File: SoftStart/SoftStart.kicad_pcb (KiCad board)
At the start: 2 copper layers, 88 x 56 mm, 26 parts, among them J1 LIVE, J10 LIVE, J2 NEUTRAL, J3 SW1, J4 SW2, J5 NEUTRAL, J6 SWOUTPUT, J7 LIVE, J8 LIVE, J9 LIVE

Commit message: Submitted to JLCPCB 2020-08-24
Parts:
- moved R3 1.00 mm to (159.0, 41.0)
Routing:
- net Net-(C1-Pad2): track 127.0 -> 126.1 mm
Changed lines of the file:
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@@
     (links 34)
     (no_connects 0)
-    (area 95.924999 24.924999 184.075001 81.075001)
+    (area 95.924999 24.924999 184.075001 81.200002)
     (thickness 1.6)
     (drawings 11)
@@
   )
   (setup
-    (last_trace_width 2)
+    (last_trace_width 0.25)
     (user_trace_width 0.5)
     (user_trace_width 1)
@@
     (pad_to_mask_clearance 0.2)
     (aux_axis_origin 0 0)
-    (visible_elements FFFFFF7F)
+    (visible_elements 7FFFFFFF)
     (pcbplotparams
       (layerselection 0x010f0_80000001)
@@
   )
   (module Resistors_THT:R_Axial_Power_L20.0mm_W6.4mm_P22.40mm (layer F.Cu)
-    (at 159 40)
+    (at 159 41)
     (descr "Resistor, Axial_Power series, Axial, Horizontal, pin pitch=22.4mm, 4W, length*diameter=20*6.4mm^2, http://cdn-reichelt.de/documents/datenblatt/B400/5WAXIAL_9WAXIAL_11WAXIAL_17WAXIAL%23YAG.pdf")
     (tags "Resistor Axial_Power series Axial Horizontal pin pitch 22.4mm 4W length 20mm diameter 6.4mm")
@@
   (segment (start 181.4 57) (end 181.4 65) (width 4) (layer B.Cu) (net 2))
   (segment (start 181.4 49) (end 181.4 57) (width 4) (layer B.Cu) (net 2))
-  (segment (start 181.4 40) (end 181.4 49) (width 4) (layer B.Cu) (net 2))
+  (segment (start 181.4 41) (end 181.4 49) (width 4) (layer B.Cu) (net 2) (status 10))
   (segment (start 152.8 28.6) (end 163.6 28.6) (width 4) (layer B.Cu) (net 2))
   (segment (start 163.6 28.6) (end 175 40) (width 4) (layer B.Cu) (net 2))
-  (segment (start 175 40) (end 181.4 40) (width 4) (layer B.Cu) (net 2))
+  (segment (start 175 40) (end 181.4 41) (width 4) (layer B.Cu) (net 2) (status 20))
   (segment (start 145.2 28.6) (end 152.8 28.6) (width 4) (layer B.Cu) (net 2))
   (segment (start 108 35) (end 108 34) (width 4) (layer B.Cu) (net 2) (status 30))
@@
   (segment (start 152.8 33.68) (end 156.68 33.68) (width 2) (layer B.Cu) (net 9))
   (segment (start 156.68 33.68) (end 159 36) (width 2) (layer B.Cu) (net 9))
-  (segment (start 159 36) (end 159 40) (width 2) (layer B.Cu) (net 9))
+  (segment (start 159 36) (end 159 41) (width 2) (layer B.Cu) (net 9) (status 20))
   (segment (start 159 49) (end 159 57) (width 4) (layer B.Cu) (net 9))
-  (segment (start 159 40) (end 159 46) (width 4) (layer B.Cu) (net 9))
+  (segment (start 159 41) (end 159 46) (width 4) (layer B.Cu) (net 9) (status 10))
   (segment (start 159 46) (end 159 49) (width 4) (layer B.Cu) (net 9))
   (segment (start 159 57) (end 159 65) (width 4) (layer B.Cu) (net 9))

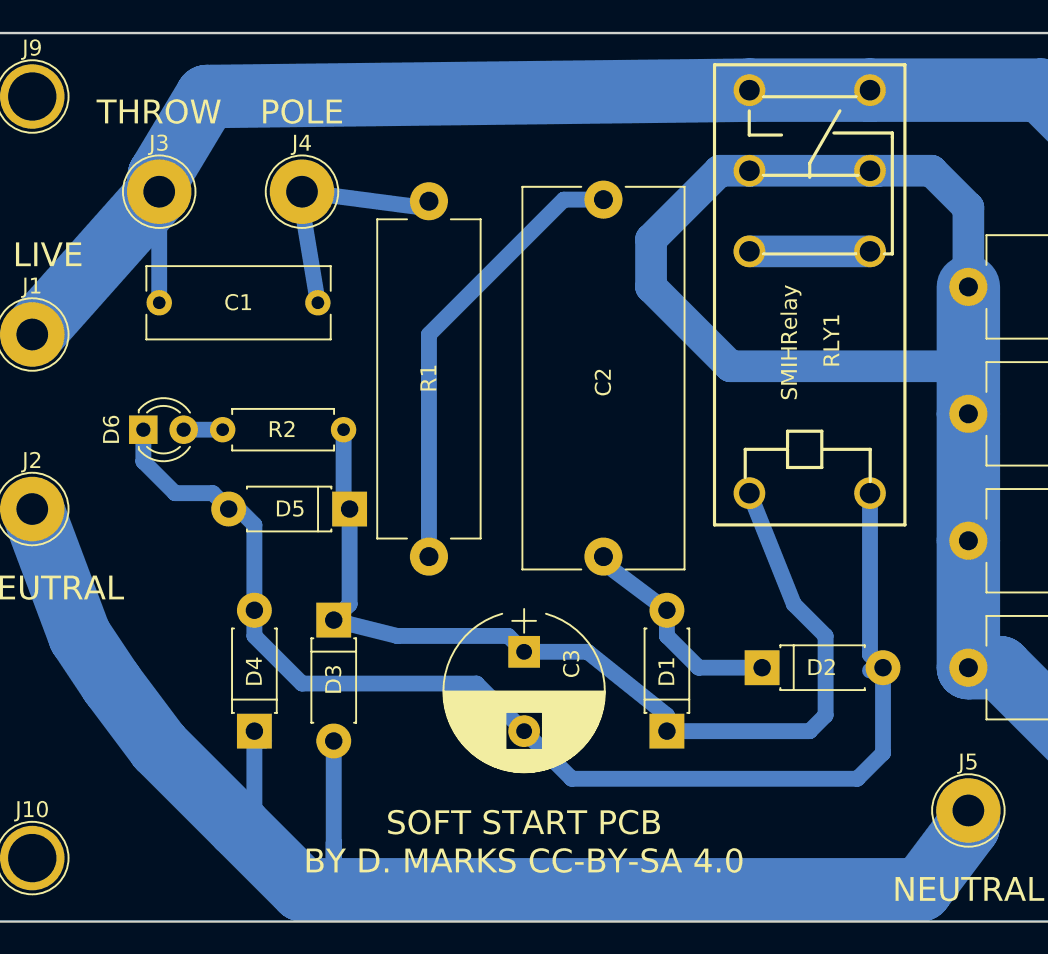
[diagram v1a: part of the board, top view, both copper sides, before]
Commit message: Fixed nasty bug in soft start
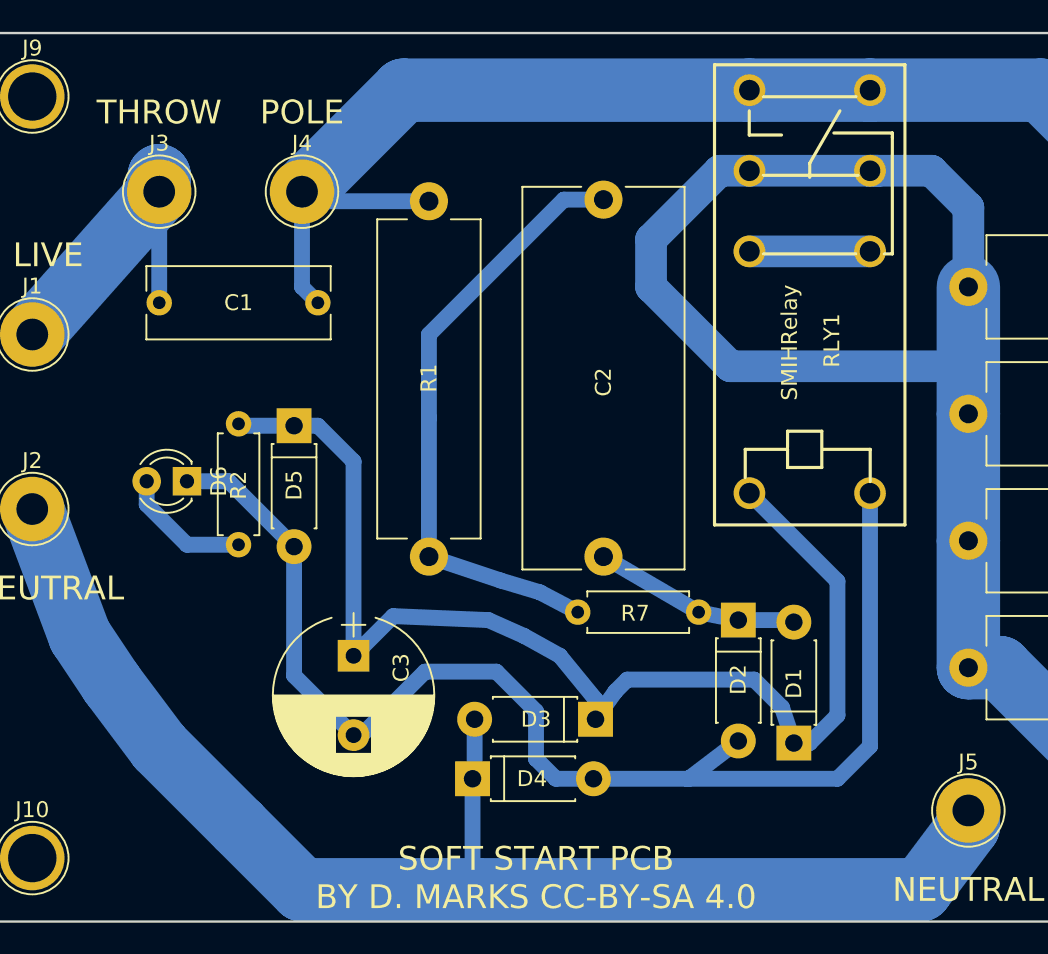
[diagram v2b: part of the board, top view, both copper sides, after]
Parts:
- added R7: 1M, Resistors_THT:R_Axial_DIN0207_L6.3mm_D2.5mm_P7.62mm_Horizontal, F.Cu at (142.0, 61.5)
- R3, R4, R5, R6: value 220R -> 150R
- moved D3 17.6 mm to (135.5, 68.2), turned to 180 degrees
- moved D4 14.1 mm to (127.8, 72.0), turned to 0 degrees
- moved C3 10.8 mm to (120.2, 64.2)
- moved D1 8.04 mm to (148.0, 69.8)
- moved R2 7.32 mm to (113.0, 57.2), turned to 90 degrees
- moved D5 6.31 mm to (116.5, 49.8), turned to 270 degrees
- moved D6 4.26 mm to (109.8, 53.2), turned to 180 degrees
- moved D2 3.35 mm to (144.5, 62.0), turned to 270 degrees
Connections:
- R3 pad 2: Net-(C1-Pad2) -> Net-(C1-Pad1)
- R4 pad 2: Net-(C1-Pad2) -> Net-(C1-Pad1)
- R5 pad 2: Net-(C1-Pad2) -> Net-(C1-Pad1)
- R6 pad 2: Net-(C1-Pad2) -> Net-(C1-Pad1)
- RLY1 pad 3: Net-(C1-Pad2) -> Net-(C1-Pad1)
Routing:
- net Net-(C1-Pad2): track 126.1 -> 21.0 mm
- net Net-(C1-Pad1): track 15.9 -> 113.1 mm
- net Net-(C3-Pad1): track 62.3 -> 75.7 mm
- net Net-(D3-Pad2): track 101.0 -> 89.2 mm
- net Net-(C2-Pad2): track 28.5 -> 39.1 mm
- net Net-(D6-Pad2): track 2.46 -> 8.30 mm
- net Net-(C3-Pad2): track 79.2 -> 81.9 mm

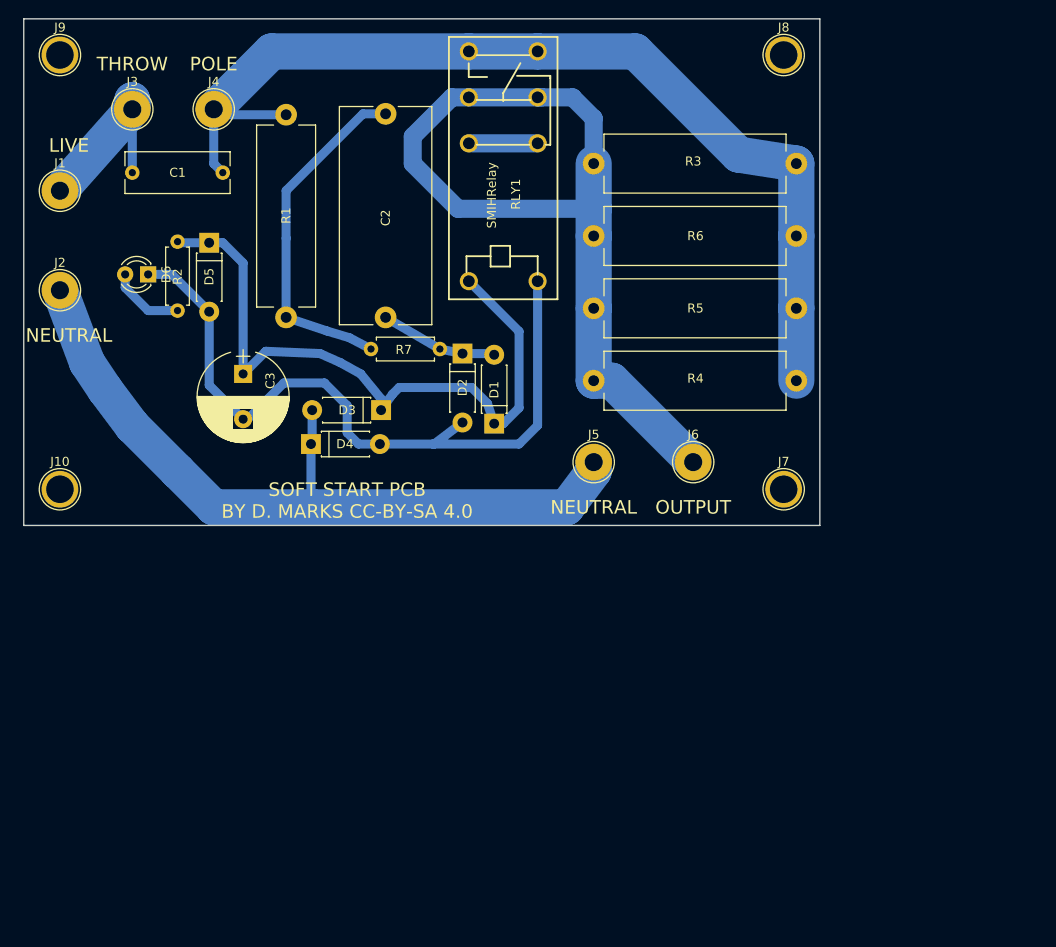
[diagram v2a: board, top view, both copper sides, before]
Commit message: Changed softstart and Poweramp to TO-220 transistors
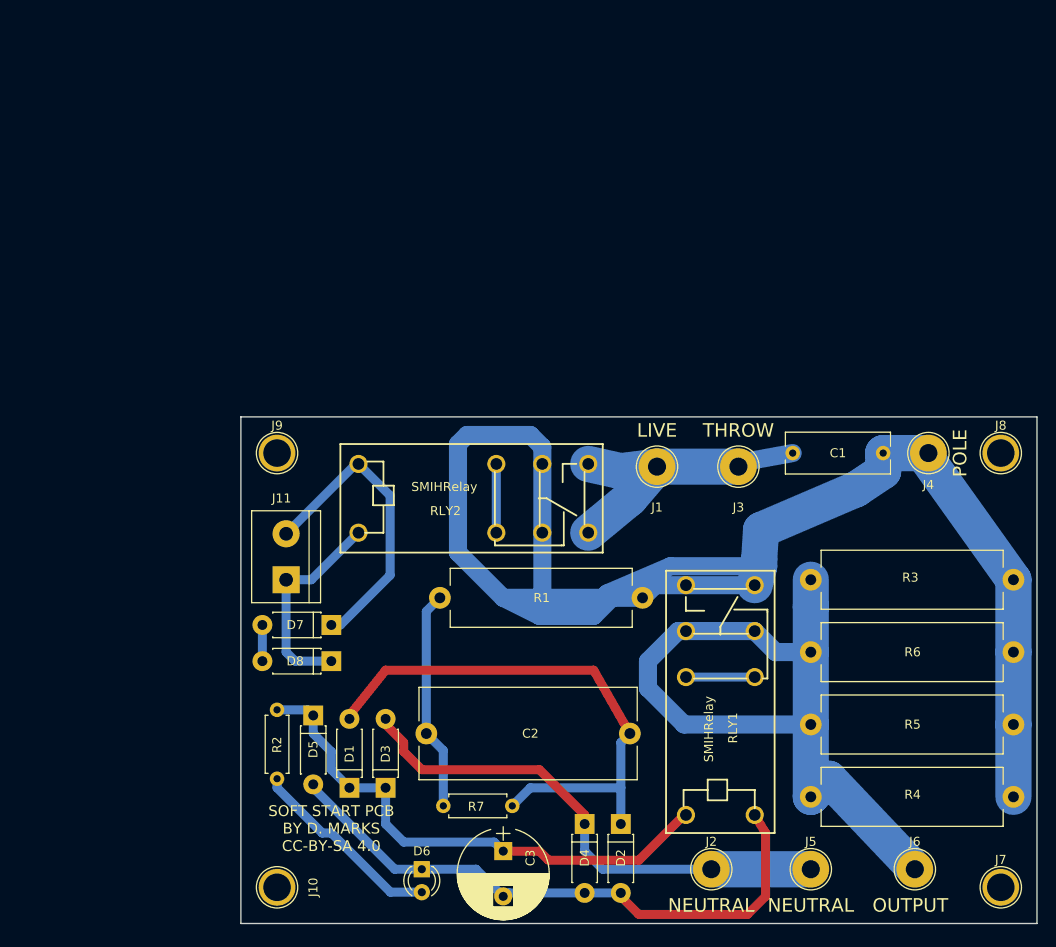
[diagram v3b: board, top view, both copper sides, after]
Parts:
- added D7: 1N4742, Diodes_THT:D_DO-41_SOD81_P7.62mm_Horizontal, F.Cu at (130.0, 92.0)
- added D8: 1N4742, Diodes_THT:D_DO-41_SOD81_P7.62mm_Horizontal, F.Cu at (130.0, 96.0)
- added J11: Conn_01x02, Connectors_Terminal_Blocks:TerminalBlock_bornier-2_P5.08mm, F.Cu at (125.0, 87.0)
- added RLY2: SPDTRelay, SoftStart:SMIHRelay, F.Cu at (143.0, 78.0)
- moved J2 96.3 mm to (172.0, 119.0)
- moved J4 87.7 mm to (196.0, 73.0)
- moved C1 79.3 mm to (191.0, 73.0)
- moved J3 77.8 mm to (175.0, 74.5)
- moved J1 72.7 mm to (166.0, 74.5)
- moved D6 72.4 mm to (140.0, 119.0), turned to 270 degrees
- moved RLY1 63.7 mm to (173.0, 103.0)
- moved C3 60.1 mm to (149.0, 117.0)
- moved D2 54.9 mm to (162.0, 114.0)
- moved D5 53.5 mm to (128.0, 102.0)
- moved C2 53.3 mm to (163.0, 104.0), turned to 180 degrees
- moved R2 52.9 mm to (124.0, 109.0)
- moved R3 51.9 mm to (183.0, 87.0)
- moved R4 51.9 mm to (183.0, 111.0)
- moved R5 51.9 mm to (183.0, 103.0)
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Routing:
- net Net-(C1-Pad1): track 113.1 -> 179.0 mm
- net Net-(C2-Pad1): track 13.4 -> 61.1 mm
- net Net-(D7-Pad1): track 0.00 -> 33.7 mm
- net Net-(D3-Pad2): track 89.2 -> 57.4 mm
- net Net-(D8-Pad1): track 0.00 -> 23.6 mm
- net Net-(C3-Pad1): track 75.7 -> 58.8 mm
- net Net-(C3-Pad2): track 81.9 -> 66.8 mm
- net Net-(C2-Pad2): track 39.1 -> 25.3 mm
- net Net-(D6-Pad2): track 8.30 -> 21.8 mm
- net Net-(C1-Pad2): track 21.0 -> 33.6 mm
- net Net-(J6-Pad1): track 92.1 -> 83.6 mm
- net Net-(RLY2-Pad2): track 0.00 -> 7.60 mm
- net Net-(D7-Pad2): track 0.00 -> 4.00 mm
